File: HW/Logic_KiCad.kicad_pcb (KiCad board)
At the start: 4 copper layers, 100 x 100 mm, 248 parts, among them J1 USB_B_Micro, Q1 Q_NPN_BEC, Q2 Q_NPN_BEC, Q4 Q_NMOS_GSD, Q5 Q_PMOS_GSD, Q6 Q_NMOS_GSD, Q7 Q_PMOS_GSD, Q8 Q_NMOS_GSD, Q9 Q_PMOS_GSD, SW1 SW_SPDT, SW10 button, SW11 button, SW12 button, SW2 button, SW3 button, SW4 button, SW5 button, SW6 button, SW7 button, SW8 button, SW9 button, U1 ESP32-PICO-D4, U2 CP2102N-A01-GQFN28, U3 SY8105

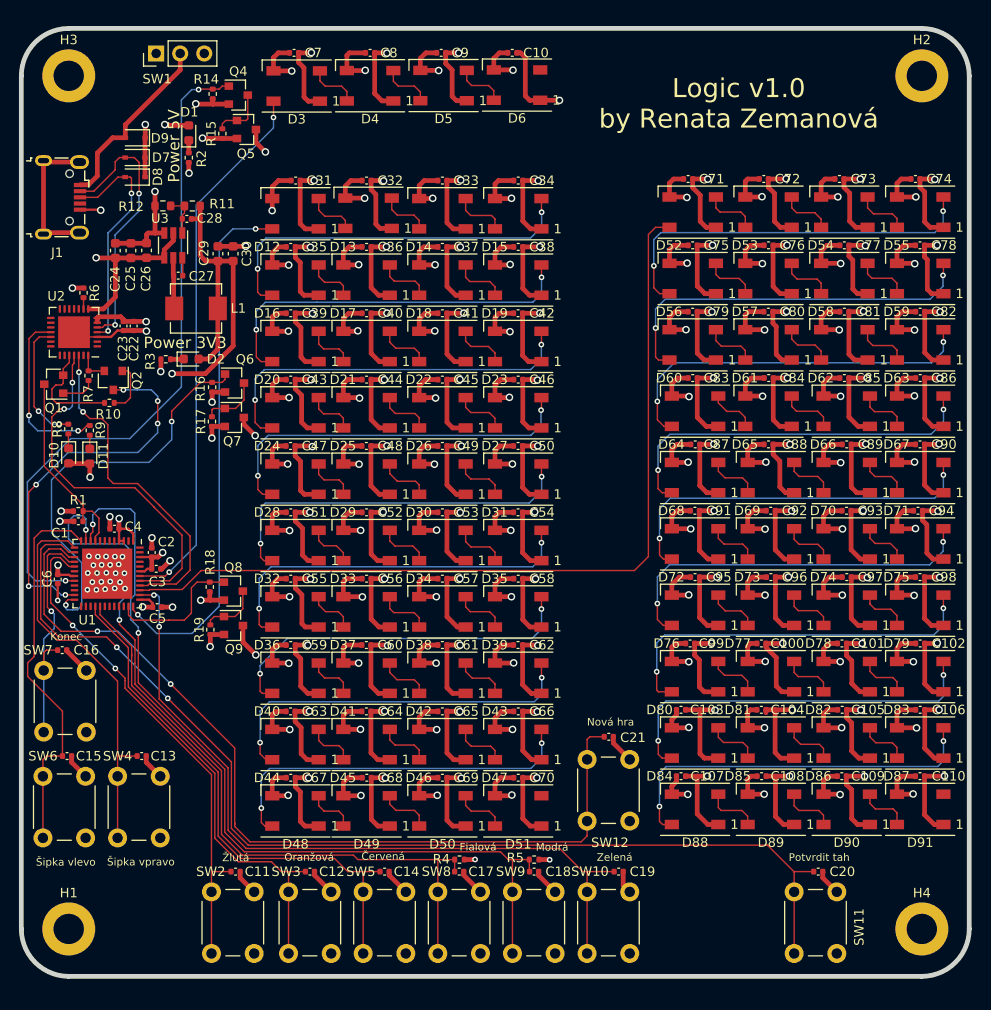
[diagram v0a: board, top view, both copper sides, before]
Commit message: V1.1 change SMD buttons, add diode on VCC
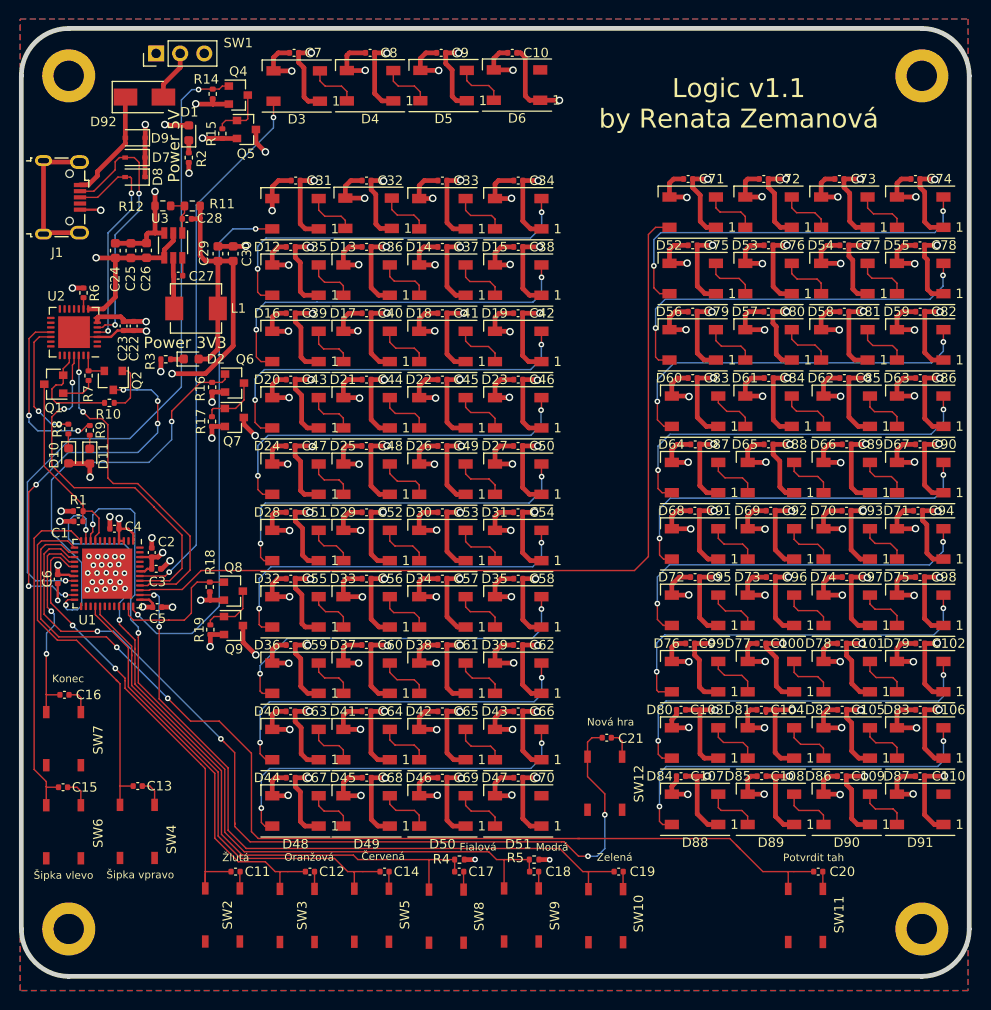
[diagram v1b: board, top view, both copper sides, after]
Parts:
- added D92: DIODE, Diode_SMD:D_SMA, F.Cu at (108.0, 42.2)
- D12, D13, D14, D15, D16, D17, D18, D19, D20, D21, D22, D23, D24, D25, D26, D27, D28, D29, D3, D30, D31, D32, D33, D34, D35, D36, D37, D38, D39, D4, D40, D41, D42, D43, D44, D45, D46, D47, D48, D49, D5, D50, D51, D52, D53, D54, D55, D56, D57, D58, D59, D6, D60, D61, D62, D63, D64, D65, D66, D67, D68, D69, D70, D71, D72, D73, D74, D75, D76, D77, D78, D79, D80, D81, D82, D83, D84, D85, D86, D87, D88, D89, D90, D91: value WS2812B -> WS2812C
- SW10, SW11, SW12, SW2, SW3, SW4, SW5, SW6, SW7, SW8, SW9: footprint Button_Switch_THT:SW_PUSH_6mm -> my_library:Tactile_switch
- moved C16 4.72 mm to (99.5, 105.3)
- moved SW10 4.46 mm to (156.7, 128.6)
- moved SW12 4.42 mm to (156.6, 114.6)
- moved SW2 4.23 mm to (116.3, 128.5)
- moved SW11 4.20 mm to (177.8, 128.6)
- moved SW9 4.18 mm to (147.8, 128.5)
- moved SW5 4.14 mm to (132.0, 128.6)
- moved SW3 4.12 mm to (124.1, 128.6)
- moved SW8 4.04 mm to (139.9, 128.7)
- moved C15 3.32 mm to (99.4, 115.0)
- moved C13 3.19 mm to (107.3, 114.9)
- moved SW6 2.29 mm to (99.5, 119.8)
- moved SW7 2.23 mm to (99.5, 109.9)
- moved SW4 2.21 mm to (107.3, 119.7)
- moved C21 0.23 mm to (156.8, 109.8)
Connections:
- SW1 pad 2: V_IN -> Net-(D92-Pad2)
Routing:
- net V_IN: track 19.5 -> 11.8 mm
- net BARVA_5: track 90.2 -> 83.4 mm
- net BARVA_2: track 49.4 -> 42.5 mm
- net BARVA_3: track 56.9 -> 50.0 mm
- net BARVA_6: track 80.9 -> 74.1 mm
- net BARVA_4: track 85.4 -> 78.6 mm
- net GND: track 515.7 -> 509.3 mm
- net Net-(D92-Pad2): track 0.00 -> 5.33 mm
- net BTN_ENTER: track 116.8 -> 111.5 mm
- net BTN_SIPKA_VLEVO: track 41.0 -> 35.7 mm
- net BARVA_1: track 53.6 -> 48.7 mm
- net BTN_END: track 26.1 -> 21.9 mm, vias 1 -> 2
- net BTN_NEW_GAME: track 94.7 -> 98.6 mm, vias 2 -> 4
- net BTN_SIPKA_VPRAVO: track 42.1 -> 38.2 mm
- added copper zone on B.Cu, net GND
- added copper zone on F.Cu, net GND
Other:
- board text added: "Logic v1.1 by Renata Zemanová"
- board text removed: "Logic v1.0 by Renata Zemanová"

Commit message: add level shifter
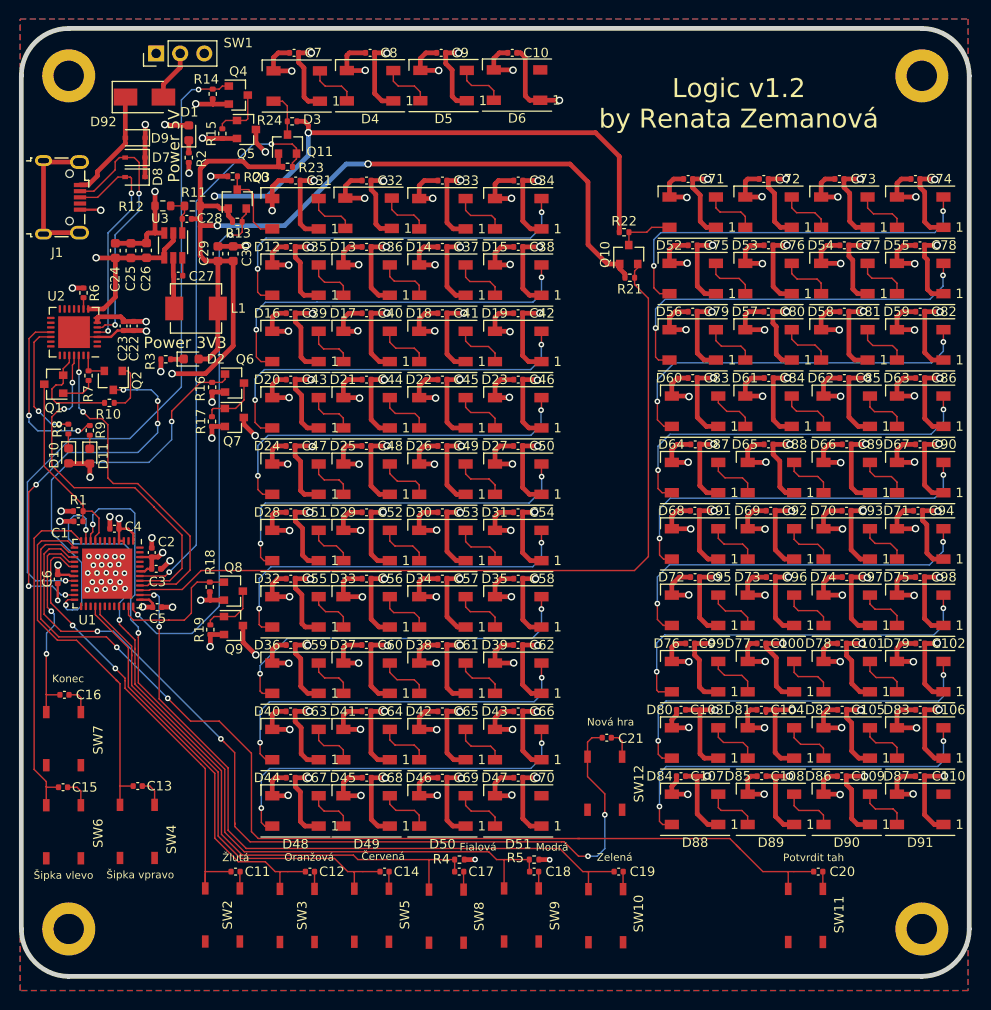
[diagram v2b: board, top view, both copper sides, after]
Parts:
- added Q10: Q_NMOS_GSD, Package_TO_SOT_SMD:SOT-23, F.Cu at (159.1, 58.9)
- added Q11: Q_NMOS_GSD, Package_TO_SOT_SMD:SOT-23, F.Cu at (123.1, 47.2)
- added Q3: Q_NMOS_GSD, Package_TO_SOT_SMD:SOT-23, F.Cu at (117.8, 53.0)
- added R13: 10k, Resistor_SMD:R_0402_1005Metric, F.Cu at (117.8, 55.4)
- added R20: 10k, Resistor_SMD:R_0402_1005Metric, F.Cu at (117.3, 50.6)
- added R21: 10k, Resistor_SMD:R_0402_1005Metric, F.Cu at (159.2, 61.3)
- added R22: 10k, Resistor_SMD:R_0402_1005Metric, F.Cu at (158.6, 56.5)
- added R23: 10k, Resistor_SMD:R_0402_1005Metric, F.Cu at (123.1, 49.6)
- added R24: 10k, Resistor_SMD:R_0402_1005Metric, F.Cu at (123.6, 44.8)
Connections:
- U1 pad 36: DATA_herni_LED -> DATA_herni_LED_LS
- U1 pad 39: DATA_hodnoceni_LED -> DATA_hodnoceni_LED_LS
- U1 pad 42: DATA_zadani_LED -> DATA_zadani_LED_LS
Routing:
- net DATA_hodnoceni_LED_LS: track 0.00 -> 86.8 mm
- net DATA_hodnoceni_LED: track 91.7 -> 5.85 mm
- net +3V3: track 69.1 -> 145.3 mm, vias 11 -> 13
- net +5V: track 29.2 -> 89.1 mm, vias 5 -> 8
- net DATA_zadani_LED_LS: track 0.00 -> 59.0 mm, vias 0 -> 2
- net DATA_herni_LED_LS: track 0.00 -> 55.6 mm, vias 0 -> 2
- net DATA_zadani_LED: track 57.5 -> 4.69 mm, vias 2 -> 0
- net DATA_herni_LED: track 56.2 -> 8.52 mm, vias 2 -> 0
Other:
- board text added: "Logic v1.2 by Renata Zemanová"
- board text removed: "Logic v1.1 by Renata Zemanová"

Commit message: add DIPS
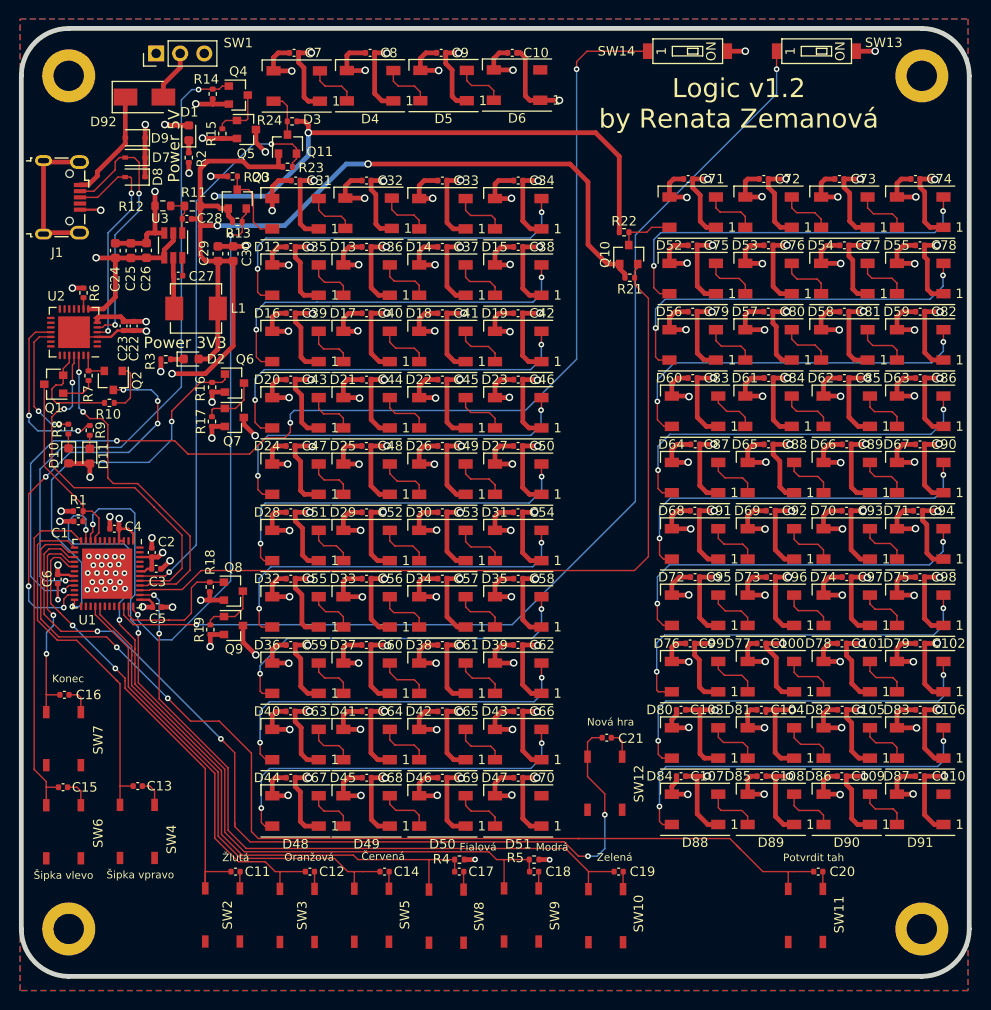
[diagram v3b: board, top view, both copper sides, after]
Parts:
- added SW13: SW_SPST, my_library:DIP1x1, F.Cu at (178.9, 37.4)
- added SW14: SW_SPST, my_library:DIP1x1, F.Cu at (165.3, 37.4)
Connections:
- U1 pad 21: Net-(U1-Pad21) -> PREPINAC_1
- U1 pad 34: Net-(U1-Pad34) -> PREPINAC_2
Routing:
- net PREPINAC_1: track 0.00 -> 121.2 mm, vias 0 -> 4
- net PREPINAC_2: track 0.00 -> 114.4 mm, vias 0 -> 2
- net GND: track 509.3 -> 513.2 mm, vias 123 -> 125
- net IO0: track 40.2 -> 42.0 mm
- net ZAPINANI_2_CAST_LED: track 43.2 -> 41.4 mm
- net ZAPINANI_1_CAST_LED: track 71.2 -> 69.5 mm

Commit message: repair footprint of DIP and USB micro, change buttons with higher fretboard
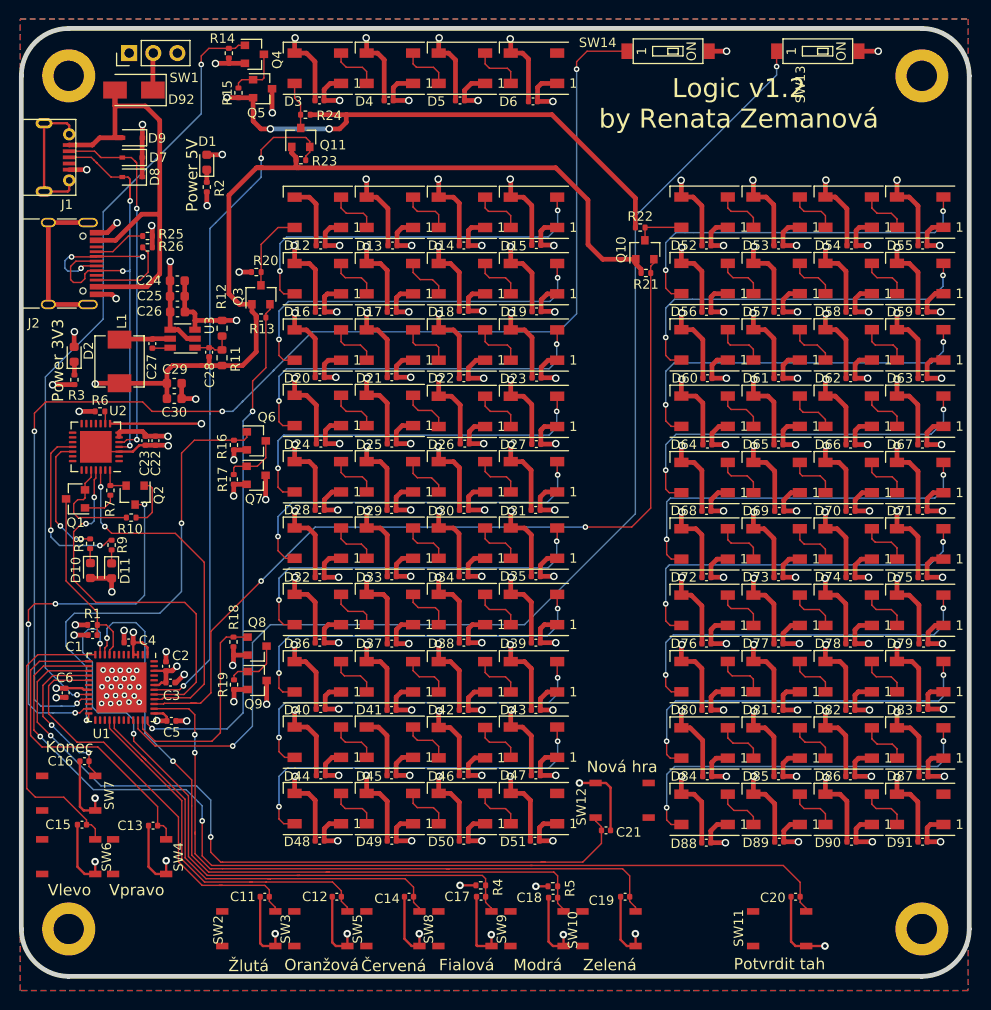
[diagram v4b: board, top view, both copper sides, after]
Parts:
- added J2: USB_C_Receptacle_USB2.0, Connector_USB:USB_C_Receptacle_HRO_TYPE-C-31-M-12, F.Cu at (98.9, 59.8)
- added R25: 5k1, Resistor_SMD:R_0402_1005Metric, F.Cu at (108.3, 56.9)
- added R26: 5k1, Resistor_SMD:R_0402_1005Metric, F.Cu at (108.3, 58.1)
- J1: footprint Connector_USB:USB_Micro-B_Wuerth_629105150521 -> my_library:USB_micro_JLCPCB_con
- moved C30 16.5 mm to (111.1, 74.0), turned to 180 degrees
- moved R11 16.3 mm to (116.2, 69.7), turned to 90 degrees
- moved C29 14.4 mm to (111.1, 72.4), turned to 180 degrees
- moved R12 14.3 mm to (116.2, 66.6), turned to 90 degrees
- moved C28 14.3 mm to (114.8, 69.2), turned to 270 degrees
- moved R6 12.6 mm to (103.3, 75.4), turned to 0 degrees
- moved D2 12.4 mm to (100.6, 69.4), turned to 90 degrees
- moved R10 12.3 mm to (106.6, 86.6)
- moved C22 12.3 mm to (109.2, 78.5)
- moved D10 12.3 mm to (102.3, 92.2)
- moved D11 12.3 mm to (104.5, 92.2)
- moved R8 12.3 mm to (102.3, 89.4)
- moved R9 12.3 mm to (104.5, 89.5)
- moved C23 12.3 mm to (108.1, 78.5)
- moved Q1 12.3 mm to (100.7, 84.6)
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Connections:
- D92 pad 1: V_IN -> Net-(D92-Pad1)
- D92 pad 2: Net-(D92-Pad2) -> V_IN
- SW1 pad 2: Net-(D92-Pad2) -> Net-(D92-Pad1)
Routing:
- net GND: track 513.2 -> 864.8 mm, vias 125 -> 137
- net V_LED_1: track 301.3 -> 175.1 mm
- net V_LED_3: track 207.4 -> 118.4 mm
- net V_LED_2: track 198.7 -> 118.1 mm
- net V_IN: track 11.8 -> 50.0 mm
- net Net-(D8-Pad2): track 24.7 -> 50.8 mm, vias 2 -> 3
- net Net-(D7-Pad2): track 28.6 -> 52.8 mm, vias 2 -> 5
- net Net-(J2-PadS1): track 0.00 -> 17.0 mm
- net BTN_NEW_GAME: track 98.6 -> 83.2 mm, vias 4 -> 2
- net +3V3: track 145.3 -> 130.1 mm, vias 13 -> 12
- net ZAPINANI_1_CAST_LED: track 69.5 -> 82.2 mm
- net DATA_zadani_LED_LS: track 59.0 -> 71.3 mm
- net PREPINAC_1: track 121.2 -> 131.8 mm
- net PREPINAC_2: track 114.4 -> 124.4 mm
- net Net-(J2-PadB5): track 0.00 -> 8.63 mm
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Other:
- board text added: "Vlevo"
- board text added: "Vpravo"
- board text removed: "Šipka vlevo"
- board text removed: "Šipka vpravo"

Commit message: change USB footprint, add 3. DIP
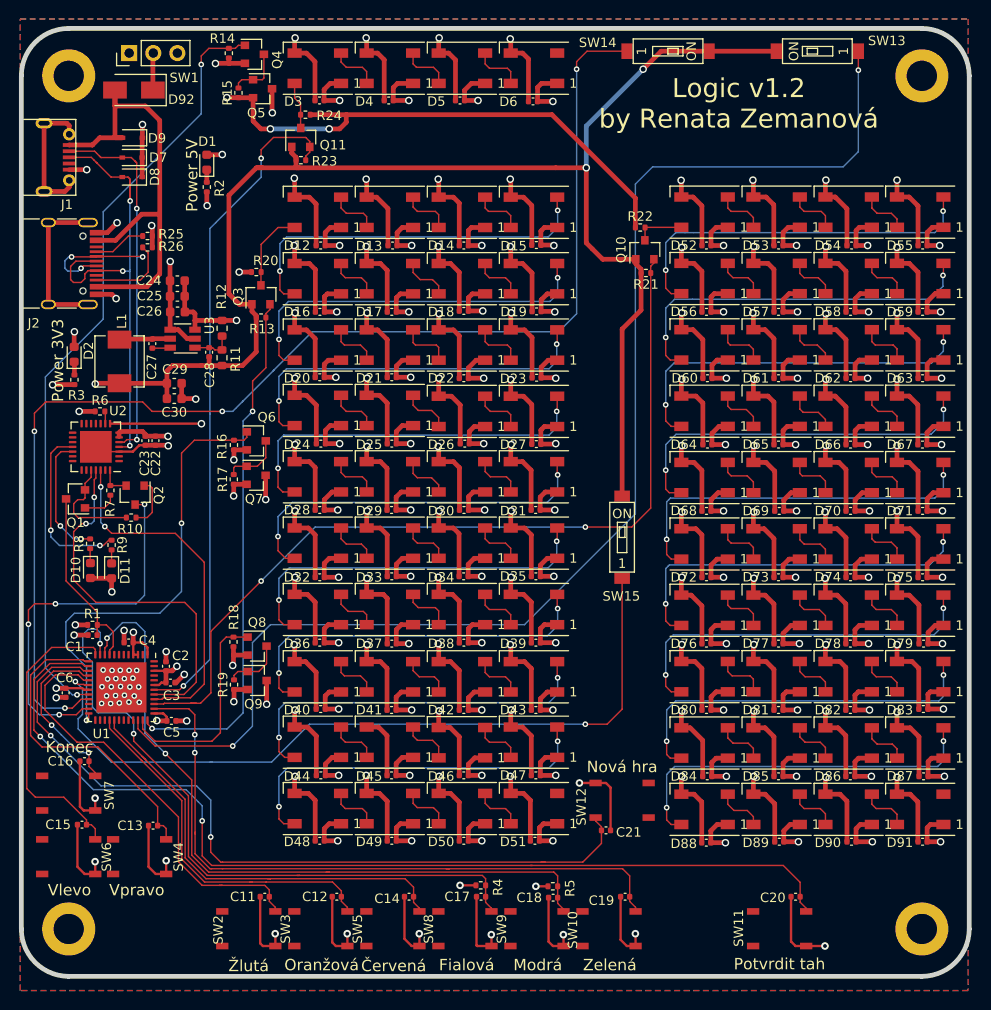
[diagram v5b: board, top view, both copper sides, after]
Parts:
- added SW15: SW_SPST, my_library:DIP1x1, F.Cu at (158.4, 88.7)
- turned SW13 to 90 degrees
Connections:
- SW13 pad 2: GND -> +3V3
- SW14 pad 2: GND -> +3V3
- U1 pad 18: Net-(U1-Pad18) -> PREPINAC_3
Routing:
- net PREPINAC_3: track 0.00 -> 82.2 mm, vias 0 -> 2
- net +3V3: track 130.1 -> 184.1 mm, vias 12 -> 14
- net PREPINAC_2: track 124.4 -> 140.3 mm
- net GND: track 864.8 -> 862.9 mm, vias 137 -> 136
- net BARVA_1: track 44.0 -> 45.0 mm
- net BARVA_5: track 76.9 -> 76.4 mm
- net BTN_SIPKA_VLEVO: track 31.1 -> 31.6 mm

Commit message: repair DIPs, add pullup and pulldown resistors
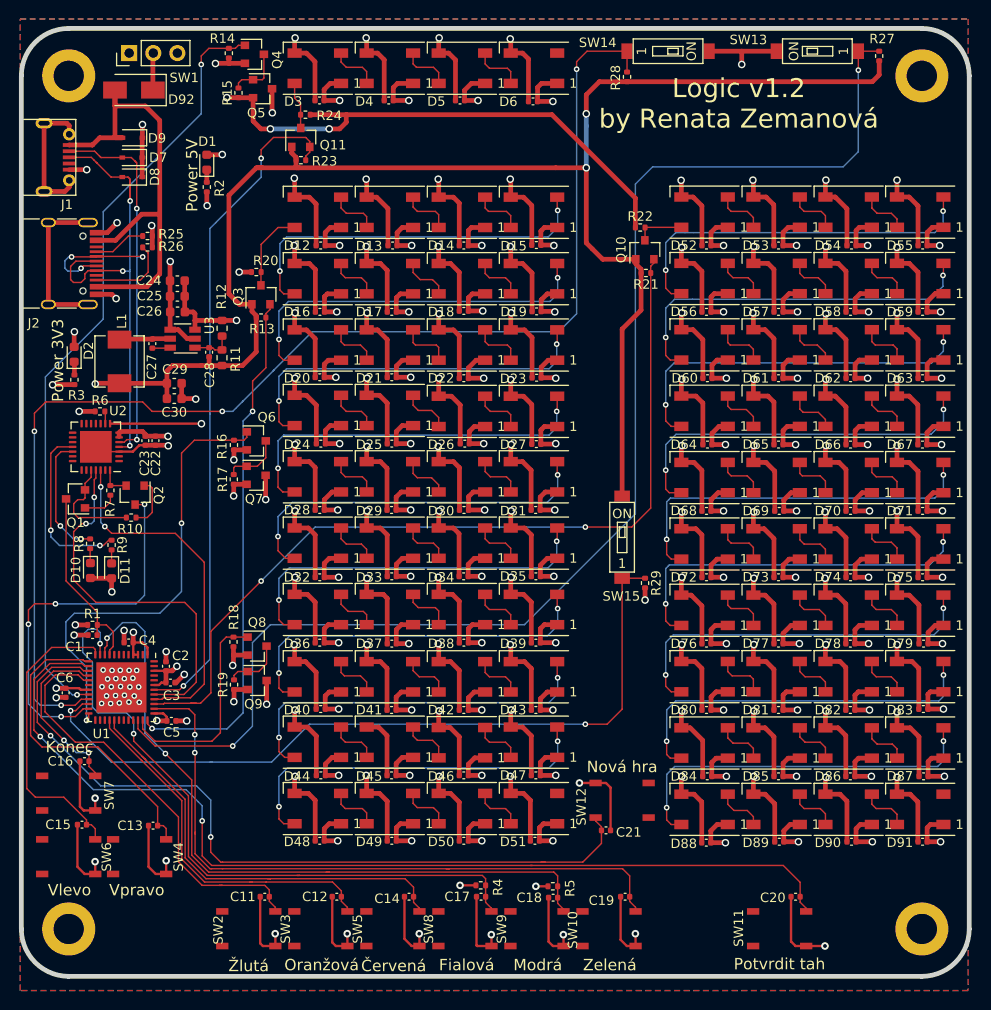
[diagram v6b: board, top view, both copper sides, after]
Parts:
- added R27: 10k, Resistor_SMD:R_0402_1005Metric, F.Cu at (185.5, 37.9)
- added R28: 10k, Resistor_SMD:R_0402_1005Metric, F.Cu at (158.9, 40.1)
- added R29: 10k, Resistor_SMD:R_0402_1005Metric, F.Cu at (160.8, 93.5)
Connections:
- SW13 pad 2: +3V3 -> GND
- SW14 pad 2: +3V3 -> GND
- U1 pad 18: PREPINAC_3 -> Net-(U1-Pad18)
- U1 pad 22: Net-(U1-Pad22) -> PREPINAC_3
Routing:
- net +3V3: track 184.1 -> 197.3 mm
- net GND: track 862.9 -> 872.6 mm, vias 136 -> 138
- net PREPINAC_2: track 140.3 -> 142.5 mm
- net PREPINAC_1: track 131.9 -> 133.8 mm
